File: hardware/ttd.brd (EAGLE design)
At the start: 55.9 x 61 mm, 20 parts, among them Q1 IRFZ44N, Q2 IRFZ44N, Q3 IRFZ44N, Q4 IRFZ44N, X1 MKDSN1,5/2-5,08, X2 MKDSN1,5/2-5,08

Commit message: kleine Verschiebungen
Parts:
- moved D6 2.54 mm to (43.2, 10.2)
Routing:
- net GND: track 188.0 -> 180.4 mm
- net N$7: track 76.2 -> 73.7 mm
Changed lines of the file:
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@@
 <element name="D4" library="diode" package="DO201T15" value="SB540" x="43.18" y="40.64" rot="R180"/>
 <element name="D5" library="diode" package="DO201T15" value="SB540" x="43.18" y="20.32"/>
-<element name="D6" library="diode" package="DO201T15" value="SB540" x="43.18" y="7.62" rot="R180"/>
+<element name="D6" library="diode" package="DO201T15" value="SB540" x="43.18" y="10.16" rot="R180"/>
 <element name="X1" library="con-phoenix-508" package="MKDSN1,5/2-5,08" value="MKDSN1,5/2-5,08" x="40.64" y="30.48" rot="R270">
 <attribute name="OC_NEWARK" value="30M2397" x="40.64" y="30.48" size="1.778" layer="27" rot="R270" display="off"/>
@@
 <wire x1="50.8" y1="25.4" x2="50.8" y2="20.32" width="1.016" layer="16"/>
 <wire x1="50.8" y1="20.32" x2="50.8" y2="12.7" width="1.016" layer="16"/>
-<wire x1="50.8" y1="7.62" x2="50.8" y2="12.7" width="1.016" layer="16"/>
+<wire x1="50.8" y1="10.16" x2="50.8" y2="12.7" width="1.016" layer="16"/>
 <wire x1="50.8" y1="12.7" x2="27.94" y2="12.7" width="1.016" layer="16"/>
 <wire x1="40.665" y1="27.9611" x2="40.64" y2="27.9611" width="1.016" layer="16"/>
@@
 <contactref element="X3" pad="4"/>
 <wire x1="30.48" y1="10.16" x2="35.56" y2="10.16" width="1.016" layer="16"/>
-<wire x1="35.56" y1="10.16" x2="35.56" y2="7.62" width="1.016" layer="16"/>
 <wire x1="35.56" y1="40.64" x2="30.48" y2="40.64" width="1.016" layer="16"/>
 <wire x1="5.08" y1="2.54" x2="35.56" y2="2.54" width="1.016" layer="16"/>
-<wire x1="35.56" y1="2.54" x2="35.56" y2="7.62" width="1.016" layer="16"/>
+<wire x1="35.56" y1="2.54" x2="35.56" y2="10.16" width="1.016" layer="16"/>
 <wire x1="5.08" y1="10.16" x2="5.08" y2="2.54" width="1.016" layer="16"/>
 <wire x1="2.54" y1="2.54" x2="5.08" y2="2.54" width="1.016" layer="16"/>
@@
 <wire x1="12.7" y1="20.32" x2="5.08" y2="20.32" width="1.016" layer="16"/>
 <wire x1="12.7" y1="20.32" x2="12.7" y2="30.48" width="1.016" layer="16"/>
-<wire x1="12.7" y1="30.48" x2="22.86" y2="30.48" width="1.016" layer="16"/>
-<wire x1="22.86" y1="30.48" x2="22.86" y2="35.56" width="1.016" layer="16"/>
-<wire x1="22.86" y1="35.56" x2="15.24" y2="35.56" width="1.016" layer="16"/>
-<wire x1="15.24" y1="35.56" x2="15.24" y2="43.18" width="1.016" layer="16"/>
+<wire x1="12.7" y1="30.48" x2="15.24" y2="30.48" width="1.016" layer="16"/>
+<wire x1="15.24" y1="30.48" x2="15.24" y2="43.18" width="1.016" layer="16"/>
 <wire x1="12.7" y1="10.16" x2="5.08" y2="10.16" width="1.016" layer="16"/>
-<wire x1="22.86" y1="30.48" x2="35.56" y2="30.48" width="1.016" layer="16"/>
+<wire x1="15.24" y1="30.48" x2="35.56" y2="30.48" width="1.016" layer="16"/>
 </signal>
 <signal name="PWM">

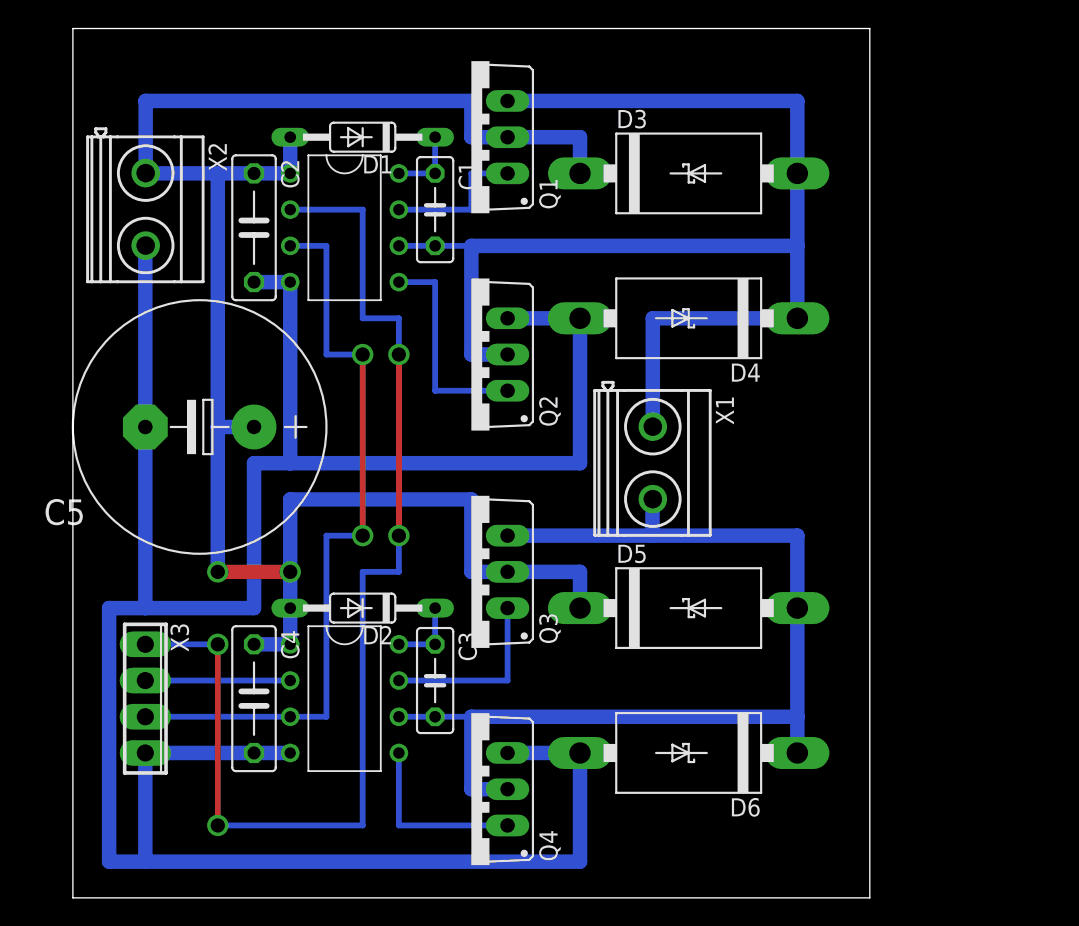
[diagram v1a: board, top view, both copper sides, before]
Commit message: Änderungen beim Aufbau im Layout nachgetragen, Bauteilwerte eingetragen
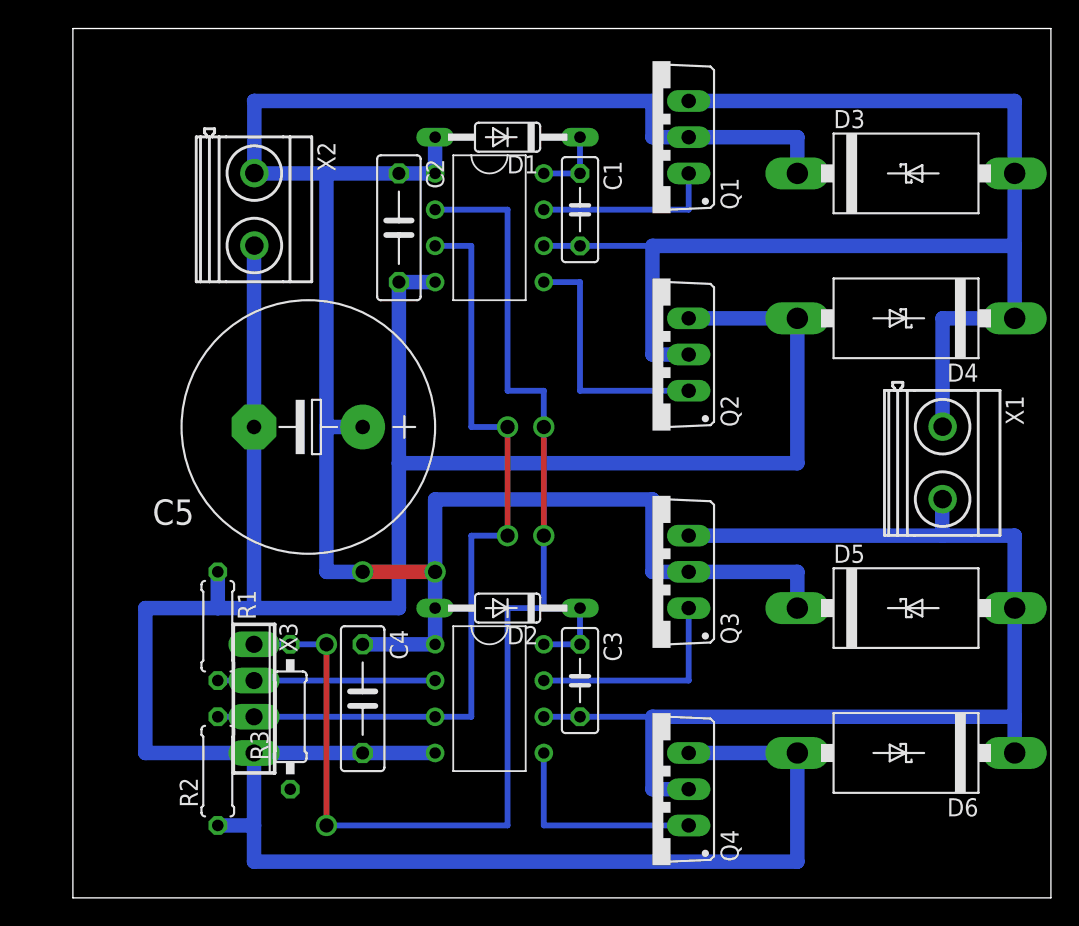
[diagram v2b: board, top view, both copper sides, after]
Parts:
- added R1, R2: 10k, resistor:0207/7
- added R3: 10k, resistor:0207/10
- C1, C3: value (none) -> 33n
- C2, C4: value (none) -> 100n
- C5: value (none) -> 2.2m
- moved X1 20.3 mm to (61.0, 30.5)
- moved D3 15.2 mm to (58.4, 50.8)
- moved D4 15.2 mm to (58.4, 40.6)
- moved D5 15.2 mm to (58.4, 20.3)
- moved D6 15.2 mm to (58.4, 10.2)
- moved Q1 12.7 mm to (40.6, 53.3)
- moved Q2 12.7 mm to (40.6, 38.1)
- moved Q3 12.7 mm to (40.6, 22.9)
- moved Q4 12.7 mm to (40.6, 7.62)
- moved C1 10.2 mm to (35.6, 48.3)
- moved C3 10.2 mm to (35.6, 15.2)
- moved C2 10.2 mm to (22.9, 47.0)
- moved D1 10.2 mm to (30.5, 53.3)
- moved D2 10.2 mm to (30.5, 20.3)
- moved U$1 10.2 mm to (29.2, 47.0)
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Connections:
- net A: now also R3.2
- net B: now also R1.2
- net GND: now also R1.1, R2.1, R3.1
- net PWM: now also R2.2
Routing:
- net GND: track 180.4 -> 210.9 mm
- net VIN: track 129.5 -> 149.8 mm
- net N$7: track 73.7 -> 81.3 mm
- net PWM: track 53.3 -> 58.4 mm
- net B: track 10.2 -> 15.2 mm
- net A: track 81.3 -> 83.8 mm
- net N$4: track 91.4 -> 93.9 mm
- net N$8: track 12.7 -> 15.2 mm
- net N$3: track 10.2 -> 12.7 mm
- net N$2: track 12.7 -> 15.2 mm
- net N$1: track 15.2 -> 17.8 mm
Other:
- board size 55.9 x 61 mm -> 68.6 x 61 mm
